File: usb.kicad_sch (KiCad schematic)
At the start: 24 parts, among them J4 CONN_02X03, U6 FT231XQ, Y1 FNETHE025

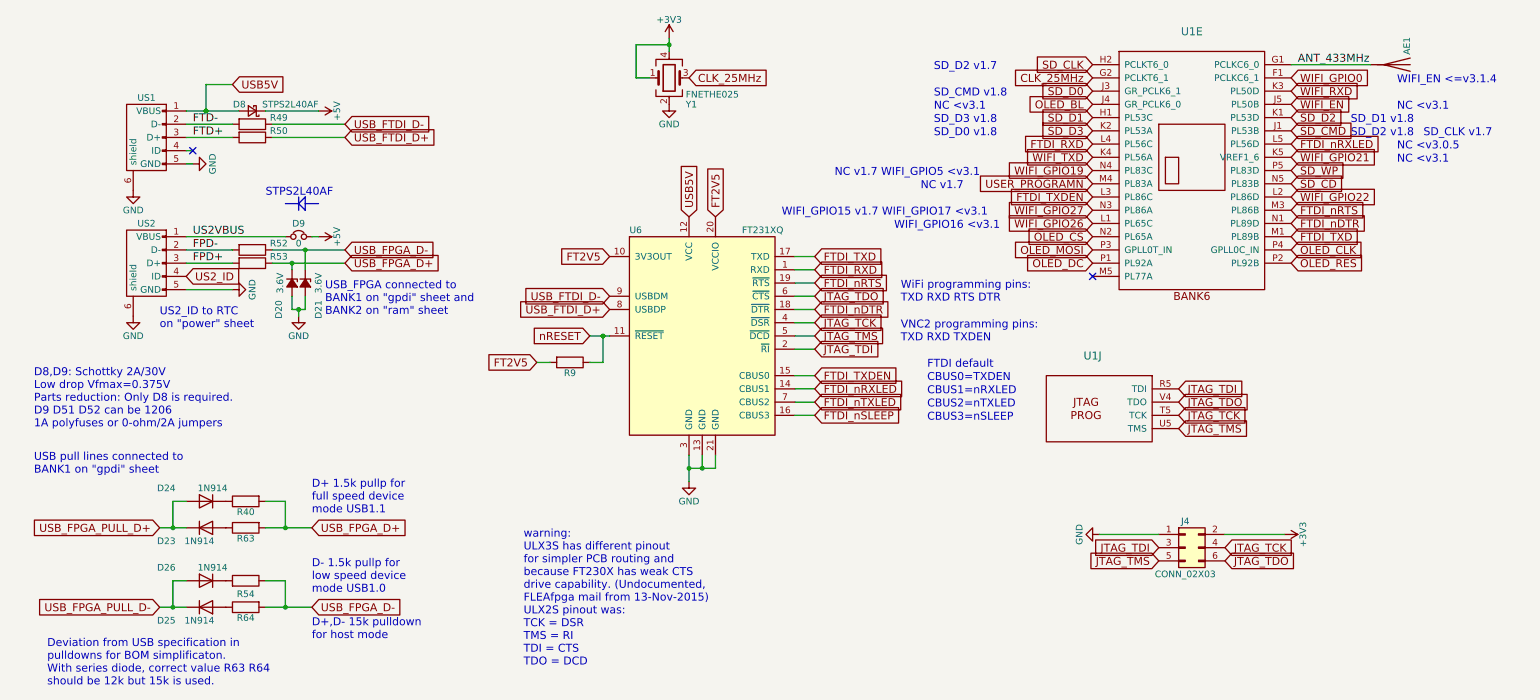
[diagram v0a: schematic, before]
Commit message: Full SerDes is now connected
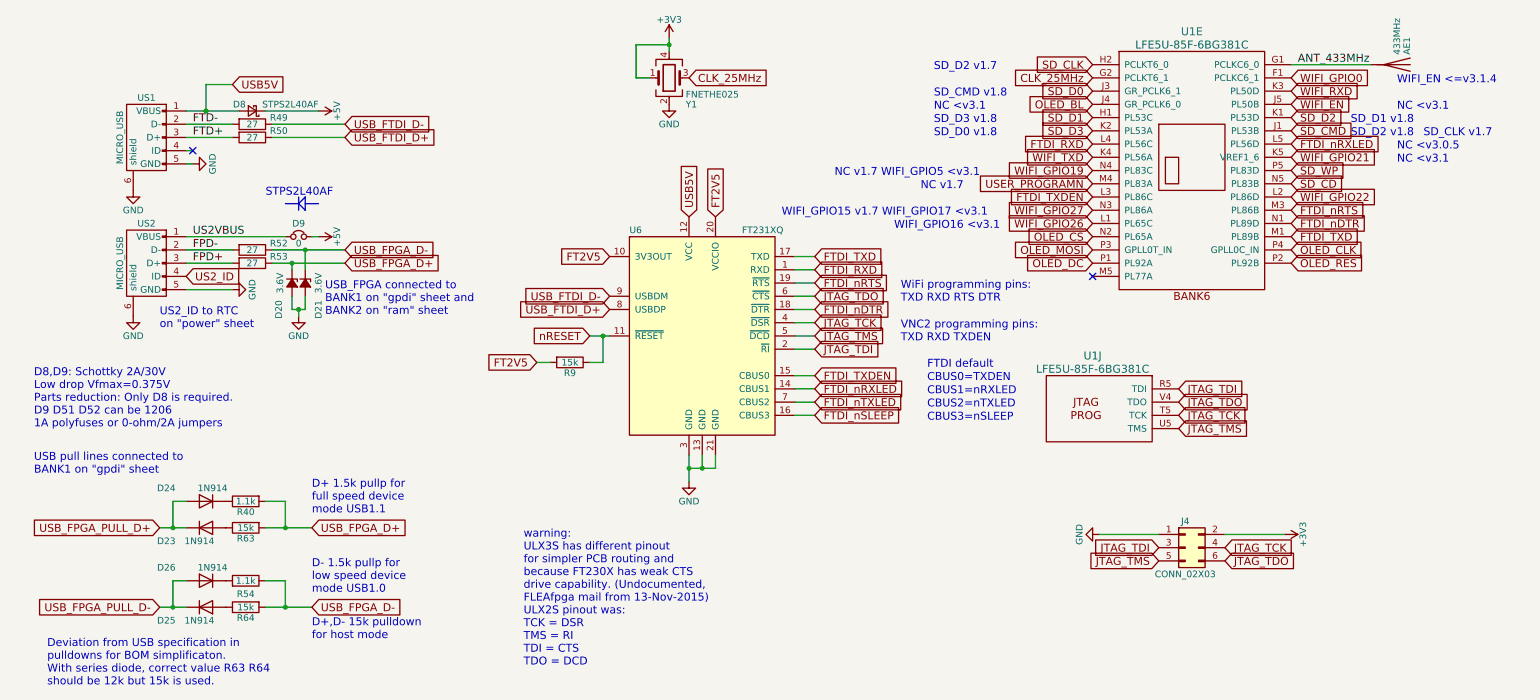
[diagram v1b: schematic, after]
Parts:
- AE1: value (none) -> 433MHz; footprint (none) -> TestPoint:TestPoint_Pad_D1.0mm
- R40, R54: value (none) -> 1.1k; footprint (none) -> Resistor_SMD:R_0603_1608Metric
- R49, R50, R52, R53: value (none) -> 27; footprint (none) -> Resistor_SMD:R_0603_1608Metric
- R63, R64, R9: value (none) -> 15k; footprint (none) -> Resistor_SMD:R_0603_1608Metric
- U1: value (none) -> LFE5U-85F-6BG381C; footprint (none) -> lfe5bg381:BGA-381_pitch0.8mm_dia0.4mm; MNF1_URL (none) -> www.latticesemi.com
- US1, US2: value (none) -> MICRO_USB; footprint (none) -> usb_otg:USB-MICRO-B-FCI-10118192-0001LF
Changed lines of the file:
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@@
     (in_bom yes) (on_board yes)
     (property "Reference" "US1" (id 0) (at 38.1 40.64 90))
-    (property "Value" "" (id 1) (at 33.02 48.26 0))
-    (property "Footprint" "" (id 2) (at 40.64 46.99 90)
+    (property "Value" "MICRO_USB" (id 1) (at 33.02 48.26 0))
+    (property "Footprint" "usb_otg:USB-MICRO-B-FCI-10118192-0001LF" (id 2) (at 40.64 46.99 90)
       (effects (font (size 1.27 1.27)) hide)
     )
@@
     (in_bom yes) (on_board yes)
     (property "Reference" "US2" (id 0) (at 38.1 64.77 90))
-    (property "Value" "" (id 1) (at 33.02 72.39 0))
-    (property "Footprint" "" (id 2) (at 40.64 71.12 90)
+    (property "Value" "MICRO_USB" (id 1) (at 33.02 72.39 0))
+    (property "Footprint" "usb_otg:USB-MICRO-B-FCI-10118192-0001LF" (id 2) (at 40.64 71.12 90)
       (effects (font (size 1.27 1.27)) hide)
     )
@@
     (in_bom yes) (on_board yes)
     (property "Reference" "R9" (id 0) (at 119.38 93.472 90))
-    (property "Value" "" (id 1) (at 119.38 91.44 90))
-    (property "Footprint" "" (id 2) (at 119.38 89.662 90)
+    (property "Value" "15k" (id 1) (at 119.38 91.44 90))
+    (property "Footprint" "Resistor_SMD:R_0603_1608Metric" (id 2) (at 119.38 89.662 90)
       (effects (font (size 1.27 1.27)) hide)
     )
@@
     (in_bom yes) (on_board yes)
     (property "Reference" "R40" (id 0) (at 57.15 120.142 90))
-    (property "Value" "" (id 1) (at 57.15 118.11 90))
-    (property "Footprint" "" (id 2) (at 57.15 116.332 90)
+    (property "Value" "1.1k" (id 1) (at 57.15 118.11 90))
+    (property "Footprint" "Resistor_SMD:R_0603_1608Metric" (id 2) (at 57.15 116.332 90)
       (effects (font (size 1.27 1.27)) hide)
     )
@@
     (in_bom yes) (on_board yes)
     (property "Reference" "R49" (id 0) (at 63.5 44.45 90))
-    (property "Value" "" (id 1) (at 58.42 45.72 90))
-    (property "Footprint" "" (id 2) (at 58.42 43.942 90)
+    (property "Value" "27" (id 1) (at 58.42 45.72 90))
+    (property "Footprint" "Resistor_SMD:R_0603_1608Metric" (id 2) (at 58.42 43.942 90)
       (effects (font (size 1.27 1.27)) hide)
     )
@@
     (in_bom yes) (on_board yes)
     (property "Reference" "R50" (id 0) (at 63.5 46.99 90))
-    (property "Value" "" (id 1) (at 58.42 48.26 90))
-    (property "Footprint" "" (id 2) (at 58.42 46.482 90)
+    (property "Value" "27" (id 1) (at 58.42 48.26 90))
+    (property "Footprint" "Resistor_SMD:R_0603_1608Metric" (id 2) (at 58.42 46.482 90)
       (effects (font (size 1.27 1.27)) hide)
     )
@@
     (in_bom yes) (on_board yes)
     (property "Reference" "R52" (id 0) (at 63.5 68.58 90))
-    (property "Value" "" (id 1) (at 58.42 69.85 90))
-    (property "Footprint" "" (id 2) (at 58.42 68.072 90)
+    (property "Value" "27" (id 1) (at 58.42 69.85 90))
+    (property "Footprint" "Resistor_SMD:R_0603_1608Metric" (id 2) (at 58.42 68.072 90)
       (effects (font (size 1.27 1.27)) hide)
     )
@@
     (in_bom yes) (on_board yes)
     (property "Reference" "R53" (id 0) (at 63.5 71.12 90))
-    (property "Value" "" (id 1) (at 58.42 72.39 90))
-    (property "Footprint" "" (id 2) (at 58.42 70.612 90)
+    (property "Value" "27" (id 1) (at 58.42 72.39 90))
+    (property "Footprint" "Resistor_SMD:R_0603_1608Metric" (id 2) (at 58.42 70.612 90)
       (effects (font (size 1.27 1.27)) hide)
     )
@@
       (effects (font (size 1.27 1.27)) (justify right))
     )
-    (property "Value" "" (id 1) (at 278.13 32.385 0)
+    (property "Value" "433MHz" (id 1) (at 278.13 32.385 0)
       (effects (font (size 1.27 1.27)) (justify right))
     )
-    (property "Footprint" "" (id 2) (at 278.13 34.29 0)
+    (property "Footprint" "TestPoint:TestPoint_Pad_D1.0mm" (id 2) (at 278.13 34.29 0)
       (effects (font (size 1.27 1.27)) hide)
     )
@@
     (in_bom yes) (on_board yes)
     (property "Reference" "R54" (id 0) (at 57.15 135.89 90))
-    (property "Value" "" (id 1) (at 57.15 133.35 90))
-    (property "Footprint" "" (id 2) (at 57.15 135.128 90)
+    (property "Value" "1.1k" (id 1) (at 57.15 133.35 90))
+    (property "Footprint" "Resistor_SMD:R_0603_1608Metric" (id 2) (at 57.15 135.128 90)
       (effects (font (size 1.27 1.27)) hide)
     )
@@
   )
   (symbol (lib_id "lfe5bg381:LFE5UM-85F-6BG381C") (at 238.76 52.07 0) (unit 5)
-    (in_bom yes) (on_board yes)
+    (in_bom yes) (on_board no)
     (property "Reference" "U1" (id 0) (at 238.76 27.94 0)
       (effects (font (size 1.524 1.524)))
     )
-    (property "Value" "" (id 1) (at 238.76 30.48 0)
+    (property "Value" "LFE5U-85F-6BG381C" (id 1) (at 238.76 30.48 0)
       (effects (font (size 1.524 1.524)))
     )
-    (property "Footprint" "" (id 2) (at 212.09 27.94 0)
-      (effects (font (size 1.524 1.524)) hide)
-    )
-    (property "Datasheet" "http://www.latticesemi.com/~/media/LatticeSemi/Documents/DataSheets/ECP5/FPGA-DS-02012.pdf" (id 3) (at 212.09 27.94 0)
+    (property "Footprint" "lfe5bg381:BGA-381_pitch0.8mm_dia0.4mm" (id 2) (at 212.09 27.94 0)
+      (effects (font (size 1.524 1.524)) hide)
+    )
+    (property "Datasheet" "http://www.latticesemi.com/~/media/LatticeSemi/Documents/ApplicationNotes/EH/TN1261.pdf?document_id=50463" (id 3) (at 212.09 27.94 0)
       (effects (font (size 1.524 1.524)) hide)
     )
     (property "MPN" "LFE5U-85F-6BG381C" (id 4) (at 238.76 52.07 0)
+      (effects (font (size 1.524 1.524)) hide)
+    )
+    (property "MNF1_URL" "www.latticesemi.com" (id 5) (at 238.76 52.07 0)
       (effects (font (size 1.524 1.524)) hide)
     )
@@
   )
   (symbol (lib_id "lfe5bg381:LFE5UM-85F-6BG381C") (at 218.44 100.33 0) (mirror y) (unit 10)
-    (in_bom yes) (on_board yes)
+    (in_bom yes) (on_board no)
     (property "Reference" "U1" (id 0) (at 219.71 90.17 0)
       (effects (font (size 1.524 1.524)))
     )
-    (property "Value" "" (id 1) (at 219.71 92.71 0)
+    (property "Value" "LFE5U-85F-6BG381C" (id 1) (at 219.71 92.71 0)
       (effects (font (size 1.524 1.524)))
     )
-    (property "Footprint" "" (id 2) (at 245.11 76.2 0)
-      (effects (font (size 1.524 1.524)) hide)
-    )
-    (property "Datasheet" "http://www.latticesemi.com/~/media/LatticeSemi/Documents/DataSheets/ECP5/FPGA-DS-02012.pdf" (id 3) (at 245.11 76.2 0)
+    (property "Footprint" "lfe5bg381:BGA-381_pitch0.8mm_dia0.4mm" (id 2) (at 245.11 76.2 0)
+      (effects (font (size 1.524 1.524)) hide)
+    )
+    (property "Datasheet" "http://www.latticesemi.com/~/media/LatticeSemi/Documents/ApplicationNotes/EH/TN1261.pdf?document_id=50463" (id 3) (at 245.11 76.2 0)
       (effects (font (size 1.524 1.524)) hide)
     )
     (property "MPN" "LFE5U-85F-6BG381C" (id 4) (at 218.44 100.33 0)
+      (effects (font (size 1.524 1.524)) hide)
+    )
+    (property "MNF1_URL" "www.latticesemi.com" (id 5) (at 218.44 100.33 0)
       (effects (font (size 1.524 1.524)) hide)
     )
@@
     (in_bom yes) (on_board yes)
     (property "Reference" "R63" (id 0) (at 57.15 125.222 90))
-    (property "Value" "" (id 1) (at 57.15 123.19 90))
-    (property "Footprint" "" (id 2) (at 57.15 121.412 90)
+    (property "Value" "15k" (id 1) (at 57.15 123.19 90))
+    (property "Footprint" "Resistor_SMD:R_0603_1608Metric" (id 2) (at 57.15 121.412 90)
       (effects (font (size 1.27 1.27)) hide)
     )
@@
     (in_bom yes) (on_board yes)
     (property "Reference" "R64" (id 0) (at 57.15 140.462 90))
-    (property "Value" "" (id 1) (at 57.15 138.43 90))
-    (property "Footprint" "" (id 2) (at 57.15 136.652 90)
-      (effects (font (size 1.27 1.27)) hide)
-    )
+    (property "Value" "15k" (id 1) (at 57.15 138.43 90))
+    (property "Footprint" "Resistor_SMD:R_0603_1608Metric" (id 2) (at 57.15 136.652 90)
+      (effects (font (size 1.27 1.27)) hide)
+    )
